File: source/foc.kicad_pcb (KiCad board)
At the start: 2 copper layers, 62.2 x 90.8 mm, 252 parts, among them J1 Conn_01x03, J2 Conn_01x06, J3 Conn_01x08, J4 NRF wireless, J5 Conn_01x04_Male, J6 TYPE-C-31-M-12, P1 SWD, Q1 MMBT5401, Q10 MMBT5401, Q11 CSD19536KCS, Q12 CSD19536KCS, Q2 MMBT5401, Q3 CSD19536KCS, Q4 CSD19536KCS, Q5 MMBT5401, Q6 MMBT5401, Q7 CSD19536KCS, Q8 CSD19536KCS, Q9 MMBT5401, SW1 SW_DPDT_x2, U1 BMI160, U10 TX4130L/PW2902, U11 MS8311, U12 MS8311, U13 MS8311, U14 TJA1050T/CM,118, U15 STM32F405RGT6, U2 AMS1117-3.3, U3 MC74VHC1G66, U4 EG3112, U5 MC74VHC1G66, U6 XL1509-5.0E1, U7 EG3112, U8 MC74VHC1G66, U9 EG3112, Y1 8MHz Crystal Resonator, X5032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

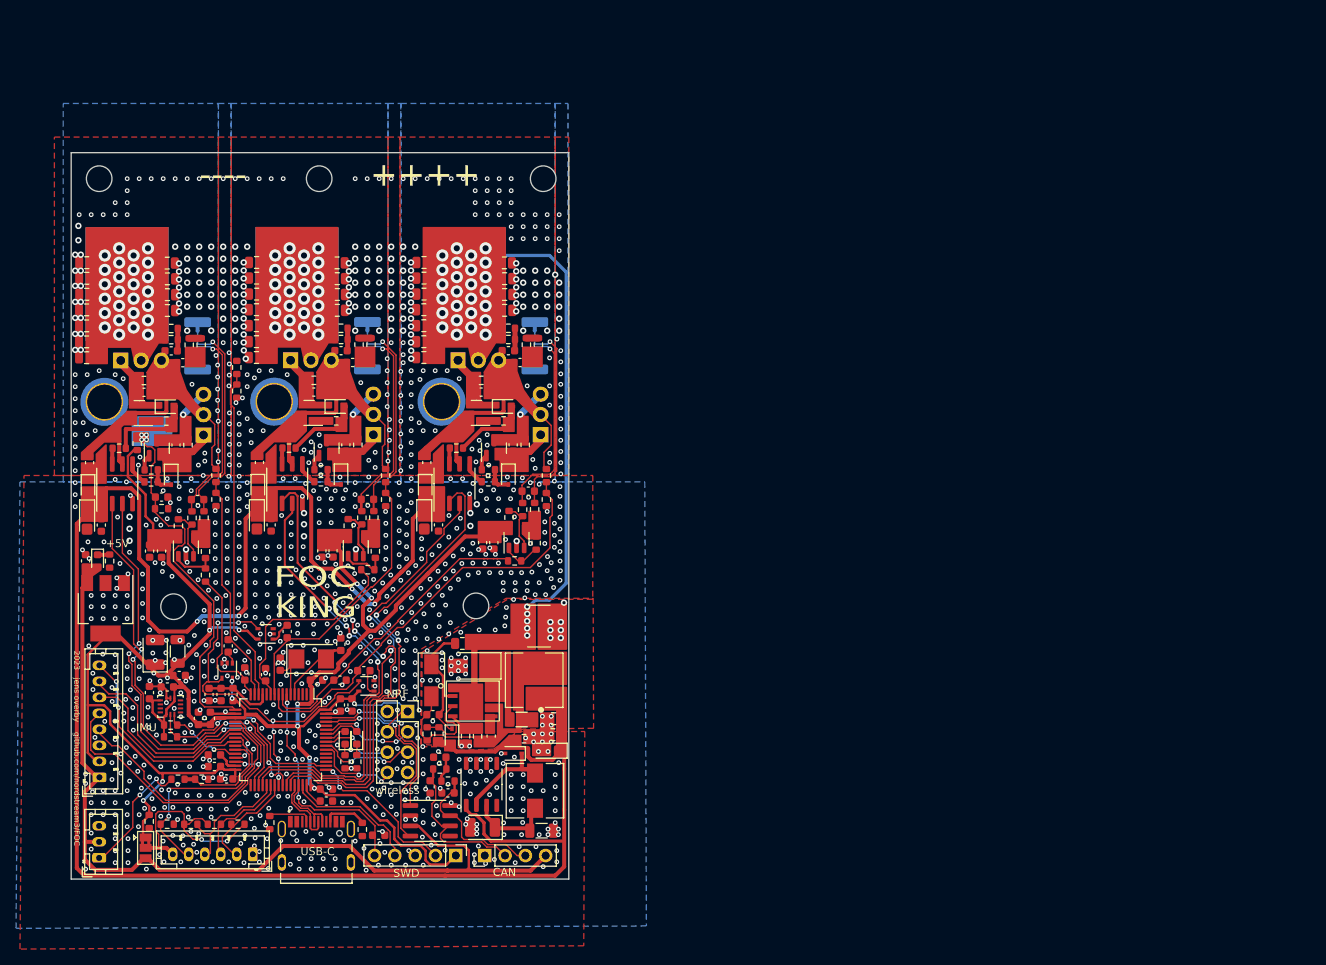
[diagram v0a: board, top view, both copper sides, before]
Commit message: 4 layer design
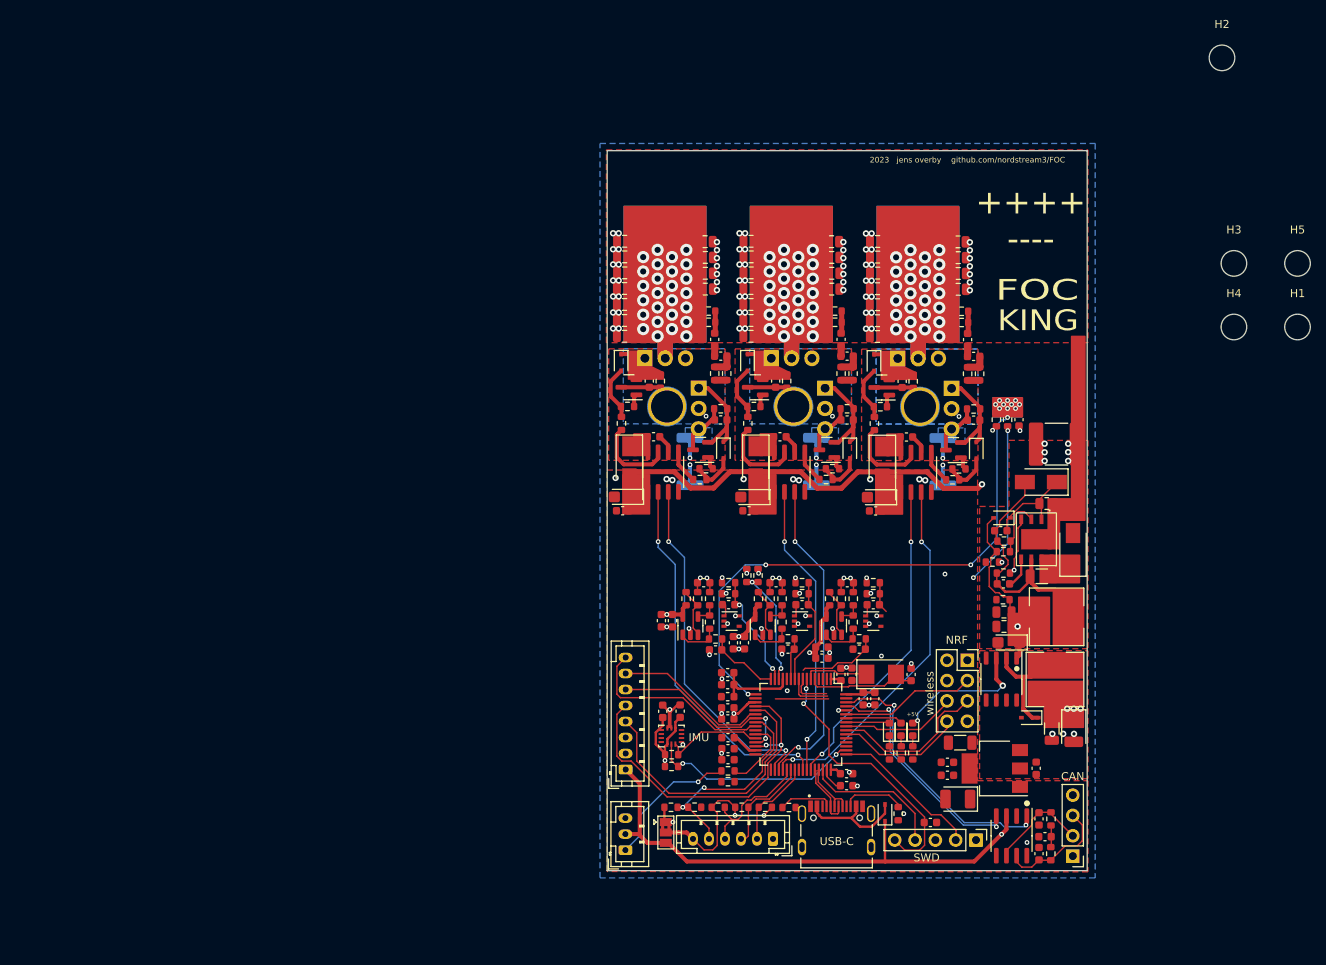
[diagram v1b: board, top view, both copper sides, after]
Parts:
- removed the C13 at (85.2, 105.9)
- removed the C20 at (106.1, 105.9)
- removed the C24 at (106.5, 99.0)
- removed the C33 at (75.1, 96.8)
- removed the C48 at (93.3, 110.0)
- removed the C52 at (92.3, 90.2)
- added C12: 2.2u, Capacitor_SMD:C_0603_1608Metric, F.Cu at (171.5, 136.4)
- added C18: 100n, Capacitor_SMD:C_0603_1608Metric, F.Cu at (162.3, 116.8)
- added C22: 2.2u, Capacitor_SMD:C_0603_1608Metric, F.Cu at (162.6, 105.0)
- added C25: 10u, Capacitor_SMD:C_0603_1608Metric, F.Cu at (166.4, 95.8)
- added C34: 2.2nF, Capacitor_SMD:C_0603_1608Metric, F.Cu at (143.2, 93.7)
- added C51: 1n, Capacitor_SMD:C_0603_1608Metric, F.Cu at (151.6, 122.3)
- added C87: 4.7n, Capacitor_SMD:C_0603_1608Metric, F.Cu at (174.8, 85.7)
- added D15: 1N5819WS, Diode_SMD:D_SOD-323, F.Cu at (163.7, 142.8)
- C11: value 1u -> 10u
- C14: value 100n -> 10u; footprint Capacitor_SMD:C_0603_1608Metric -> Capacitor_Tantalum_SMD:CP_EIA-3216-10_Kemet-I
- C15: value 2.2u -> 100n
- C16: value 1u -> 2.2u
- C17: value 100n -> 10u
- C21: value 2.2u -> 10u; footprint Capacitor_SMD:C_0603_1608Metric -> Capacitor_Tantalum_SMD:CP_EIA-3216-10_Kemet-I
- C49, C69: value 100n -> 2.2u
- C50, C70: value 1n -> 100n
- C54, C73: value 100p -> 2.2nF
- C55, C74: value 100n 100V -> 100p; footprint Capacitor_SMD:C_0805_2012Metric -> Capacitor_SMD:C_0603_1608Metric
- C66, C85: value 4.7n -> 100n 100V; footprint Capacitor_SMD:C_0603_1608Metric -> Capacitor_SMD:C_0805_2012Metric
- C68: value 2.2u -> 4.7n
- C71: value 2.2nF -> 1n
- D1, D3, D6: value 1N4148WS -> US1M; footprint Diode_SMD:D_SOD-323 -> Diode_SMD:D_SMA
- H6: value MountingHole -> Phase_A_Pad; footprint MountingHole:MountingHole_4.3mm_M4_Pad_TopOnly -> Custom:MountingHole_3.5mm_Pad_TopOnly_custom
- H7: value MountingHole -> Phase_B_Pad; footprint MountingHole:MountingHole_4.3mm_M4_Pad_TopOnly -> Custom:MountingHole_3.5mm_Pad_TopOnly_custom
- H8: value MountingHole -> Phase_C_Pad; footprint MountingHole:MountingHole_4.3mm_M4_Pad_TopOnly -> Custom:MountingHole_3.5mm_Pad_TopOnly_custom
- Q11, Q12, Q3, Q4, Q7, Q8: footprint Package_TO_SOT_THT:TO-220-3_Vertical -> Custom:TO-220-3_Vertical_bend
- moved H1 144.8 mm to (215.3, 82.0)
- moved H4 143.0 mm to (207.3, 82.0)
- moved C6 121.6 mm to (182.6, 137.2), turned to 90 degrees
- moved H2 115.7 mm to (205.8, 48.4)
- moved H3 114.8 mm to (207.3, 74.1)
- moved U2 112.9 mm to (177.4, 137.2), turned to 180 degrees
- moved R40 108.8 mm to (179.1, 93.6)
- moved C52 107.6 mm to (180.5, 93.6), turned to 90 degrees
- moved R46 104.9 mm to (177.7, 93.6), turned to 90 degrees
- moved D17 104.0 mm to (167.2, 132.3), turned to 90 degrees
- moved R79 103.2 mm to (167.2, 135.3)
- moved C8 102.0 mm to (172.8, 141.1), turned to 180 degrees
- moved C10 98.5 mm to (173.1, 134.0), turned to 180 degrees
- moved C13 96.8 mm to (171.5, 138.1), turned to 180 degrees
- moved H5 94.9 mm to (215.3, 74.1)
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- renumbered C99 to C100, C100 to C101, C101 to C102, C102 to C103, C103 to C104, C104 to C105, C12 to C13, C18 to C19, C19 to C20, C22 to C23, C23 to C24, C25 to C26, C26 to C27, C27 to C28, C28 to C29, C29 to C30, C30 to C31, C31 to C32, C32 to C33, C34 to C35, C35 to C36, C36 to C37, C37 to C38, C38 to C39, C39 to C40, C40 to C41, C41 to C42, C42 to C43, C43 to C44, C44 to C45, C45 to C46, C46 to C47, C47 to C48, C51 to C52, C87 to C88, C88 to C89, C89 to C90, C90 to C91, C91 to C92, C92 to C93, C93 to C94, C94 to C95, C95 to C96, C96 to C97, C97 to C98, C98 to C99, D15 to D16, D16 to D17
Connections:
- C14 pad 1: /driver/SENS_2 -> +12V
- C15 pad 1: +12V -> /driver/SENS_2
- C15 pad 2: Net-(C13-Pad2) -> Net-(C15-Pad2)
- C16 pad 1: Net-(C16-Pad1) -> +12V
- C16 pad 2: /driver/HS2 -> Net-(C14-Pad2)
- C17 pad 1: /driver/SENS_3 -> Net-(C17-Pad1)
- C17 pad 2: Net-(C17-Pad2) -> /driver/HS2
- C50 pad 2: /mcu/CURRENT_2 -> VCC
- C53 pad 2: Net-(C53-Pad2) -> /driver/HS2
- C55 pad 1: V_IN -> Net-(C55-Pad1)
- C55 pad 2: GND -> Net-(C55-Pad2)
- C66 pad 1: /driver/HS2 -> V_IN
- C66 pad 2: Net-(C66-Pad2) -> GND
- C68 pad 1: VCC -> /driver/HS2
- C68 pad 2: GND -> Net-(C68-Pad2)
- C70 pad 1: GND -> VCC
- C70 pad 2: /mcu/CURRENT_3 -> GND
- C71 pad 1: Net-(C71-Pad1) -> GND
- C71 pad 2: /driver/HS3 -> /mcu/CURRENT_3
- C72 pad 2: Net-(C72-Pad2) -> /driver/HS3
- C74 pad 1: V_IN -> Net-(C74-Pad1)
- C74 pad 2: GND -> Net-(C74-Pad2)
- C85 pad 1: /driver/HS3 -> V_IN
- C85 pad 2: Net-(C85-Pad2) -> GND
- D10 pad 1: Net-(C52-Pad1) -> Net-(C53-Pad1)
- D11 pad 1: Net-(C53-Pad1) -> Net-(C54-Pad1)
- D12 pad 1: Net-(C71-Pad1) -> Net-(C72-Pad1)
- D13 pad 1: Net-(C72-Pad1) -> Net-(C73-Pad1)
- D3 pad 1: Net-(C16-Pad1) -> Net-(C17-Pad1)
- H6 pad 1: (no net) -> /driver/HS1
- H7 pad 1: (no net) -> /driver/HS2
- H8 pad 1: (no net) -> /driver/HS3
- J6 pad A4B9: unconnected-(J6-PadA4B9) -> Net-(D15-Pad2)
- J6 pad B4A9: unconnected-(J6-PadB4A9) -> Net-(D15-Pad2)
- NT3 pad 1: Net-(C54-Pad2) -> Net-(C55-Pad2)
- NT3 pad 2: Net-(C53-Pad2) -> Net-(C54-Pad2)
- NT4 pad 1: Net-(C54-Pad1) -> Net-(C55-Pad1)
- NT5 pad 1: Net-(C73-Pad2) -> Net-(C74-Pad2)
- NT5 pad 2: Net-(C72-Pad2) -> Net-(C73-Pad2)
- NT6 pad 1: Net-(C73-Pad1) -> Net-(C74-Pad1)
- Q10 pad 2: Net-(C72-Pad1) -> Net-(C73-Pad1)
- Q10 pad 3: Net-(C72-Pad2) -> Net-(C73-Pad2)
- Q11 pad 1: Net-(C71-Pad1) -> Net-(C72-Pad1)
- Q12 pad 1: Net-(C72-Pad1) -> Net-(C73-Pad1)
- Q12 pad 3: Net-(C72-Pad2) -> Net-(C73-Pad2)
- Q5 pad 2: Net-(C52-Pad1) -> Net-(C53-Pad1)
- Q6 pad 2: Net-(C53-Pad1) -> Net-(C54-Pad1)
- Q6 pad 3: Net-(C53-Pad2) -> Net-(C54-Pad2)
- Q7 pad 1: Net-(C52-Pad1) -> Net-(C53-Pad1)
- Q8 pad 1: Net-(C53-Pad1) -> Net-(C54-Pad1)
- Q8 pad 3: Net-(C53-Pad2) -> Net-(C54-Pad2)
- Q9 pad 2: Net-(C71-Pad1) -> Net-(C72-Pad1)
- R48 pad 1: Net-(C54-Pad2) -> Net-(C55-Pad2)
- R49 pad 1: Net-(C54-Pad1) -> Net-(C55-Pad1)
- R50 pad 2: Net-(C52-Pad1) -> Net-(C53-Pad1)
- R51 pad 1: Net-(C53-Pad2) -> Net-(C54-Pad2)
- R51 pad 2: Net-(C53-Pad1) -> Net-(C54-Pad1)
- R52 pad 1: Net-(C53-Pad2) -> Net-(C54-Pad2)
- R53 pad 1: Net-(C66-Pad2) -> Net-(C67-Pad2)
- R54 pad 1: Net-(C67-Pad2) -> Net-(C68-Pad2)
- R55 pad 1: Net-(C66-Pad2) -> Net-(C67-Pad2)
- R56 pad 1: Net-(C67-Pad2) -> Net-(C68-Pad2)
- R64 pad 1: Net-(C73-Pad2) -> Net-(C74-Pad2)
- R65 pad 1: Net-(C73-Pad1) -> Net-(C74-Pad1)
- R66 pad 2: Net-(C71-Pad1) -> Net-(C72-Pad1)
- R67 pad 1: Net-(C72-Pad2) -> Net-(C73-Pad2)
- R67 pad 2: Net-(C72-Pad1) -> Net-(C73-Pad1)
- R68 pad 1: Net-(C72-Pad2) -> Net-(C73-Pad2)
- R69 pad 1: Net-(C85-Pad2) -> Net-(C86-Pad2)
- R70 pad 1: Net-(C86-Pad2) -> Net-(C87-Pad2)
- R71 pad 1: Net-(C85-Pad2) -> Net-(C86-Pad2)
- R72 pad 1: Net-(C86-Pad2) -> Net-(C87-Pad2)
- U5 pad 1: Net-(C14-Pad2) -> Net-(C15-Pad2)
- U7 pad 8: Net-(C16-Pad1) -> Net-(C17-Pad1)
- U8 pad 1: Net-(C17-Pad2) -> Net-(C18-Pad2)
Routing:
- net VCC: track 261.4 -> 67.8 mm, vias 13 -> 11
- net +12V: track 265.5 -> 86.3 mm, vias 4 -> 2
- net V_IN: track 75.9 -> 1.63 mm, vias 83 -> 82
- net /driver/SENS_3: track 53.7 -> 9.59 mm
- net /driver/SENS_FILTER: track 47.7 -> 6.65 mm, vias 6 -> 0
- net +5V: track 125.7 -> 86.4 mm, vias 0 -> 6
- net /driver/SENS_SUPPLY: track 41.8 -> 13.7 mm, vias 0 -> 2
- net Net-(C74-Pad2): track 0.00 -> 24.3 mm, vias 0 -> 2
- net /driver/H2: track 60.9 -> 36.8 mm, vias 4 -> 2
- net Net-(C74-Pad1): track 0.00 -> 23.7 mm, vias 0 -> 2
- net /mcu/CURRENT_3: track 38.1 -> 15.0 mm
- net /driver/SENS_2: track 35.6 -> 13.4 mm
- net /mcu/CURRENT_2: track 26.6 -> 5.08 mm
- net Net-(C55-Pad2): track 0.00 -> 21.5 mm, vias 0 -> 2
- net Net-(C54-Pad2): track 28.3 -> 6.79 mm, vias 1 -> 0
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- added copper zone on In2.Cu, net +12V
- added copper zone on In2.Cu, net +5V
- added copper zone on B.Cu, net /driver/HS1
- added copper zone on F.Cu, net /driver/HS1
- added copper zone on B.Cu, net /driver/HS2
- added copper zone on F.Cu, net /driver/HS2
- added copper zone on B.Cu, net /driver/HS3
- added copper zone on F.Cu, net /driver/HS3
- added copper zone on In2.Cu, net GND
- added copper zone on B.Cu, net Net-(C34-Pad2)
- added copper zone on In2.Cu, net VCC
- added copper zone on F.Cu, net V_IN
- added copper zone on In2.Cu, net V_IN
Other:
- board size 62.2 x 90.8 mm -> 60 x 90 mm
- copper layers 2 -> 4

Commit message: Add files via upload
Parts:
- moved H1 84.0 mm to (132.7, 66.7)
- moved H4 66.8 mm to (146.2, 108.9)
- moved H5 55.9 mm to (171.6, 108.9)
- moved H3 47.6 mm to (160.3, 66.7)
- moved H2 27.4 mm to (185.5, 66.7)
- moved C81 13.5 mm to (172.0, 73.4), turned to 0 degrees
- moved C62 13.5 mm to (156.2, 73.4), turned to 0 degrees
- moved C43 9.44 mm to (140.4, 73.4), turned to 0 degrees
- moved C45 4.02 mm to (140.4, 75.3)
- moved C63 4.02 mm to (156.2, 75.3)
- moved C82 3.99 mm to (172.0, 75.3)
- moved C41 3.95 mm to (140.4, 77.2)
- moved C64 3.95 mm to (156.2, 77.2)
- moved C83 3.93 mm to (172.0, 77.2)
- moved R35 3.92 mm to (143.8, 83.3), turned to 90 degrees
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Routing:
- net GND: track 30.7 -> 73.8 mm, vias 112 -> 95
- net Net-(J1-Pad1): track 0.00 -> 17.0 mm, vias 0 -> 1
- net VCC: track 67.8 -> 60.0 mm, vias 11 -> 10
- net V_IN: track 1.63 -> 0.18 mm, vias 82 -> 54
- net /driver/L3: track 45.6 -> 44.7 mm
- added copper zone on B.Cu, net V_IN
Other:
- board size 60 x 90 mm -> 60 x 86.7 mm
- board text added: "+++"
- board text added: "---"
- board text added: "HALL"
- board text added: "SERVO"
- board text removed: "++++"
- board text removed: "----"

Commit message: First 4 layer order at JLCPCB
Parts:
- removed the J4 at (174.0, 123.7)
- moved C69 6.60 mm to (154.9, 116.9)
- moved C49 4.80 mm to (146.0, 116.9), turned to 0 degrees
- moved U5 4.21 mm to (153.7, 123.0)
- moved C15 4.21 mm to (153.7, 121.0)
- moved C70 3.90 mm to (154.9, 118.3)
- moved C9 3.69 mm to (144.7, 120.4)
- moved U3 3.66 mm to (144.8, 122.5)
- moved C50 3.26 mm to (146.0, 118.2), turned to 0 degrees
- moved C18 3.13 mm to (162.4, 119.9)
- moved U8 3.13 mm to (162.4, 121.9)
- moved C32 2.94 mm to (139.6, 122.1)
- moved C51 2.93 mm to (148.7, 122.1)
- moved C71 2.88 mm to (157.6, 122.1)
- moved R9 2.33 mm to (144.7, 113.1), turned to 90 degrees
- moved C30 2.19 mm to (136.9, 116.9), turned to 0 degrees
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- renumbered J5 to J4, J6 to J5
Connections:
- C14 pad 2: Net-(C14-Pad2) -> GND
- C16 pad 2: Net-(C14-Pad2) -> GND
- U15 pad 29: /mcu/TX_SCL_MOSI -> unconnected-(U15-Pad29)
- U15 pad 30: /mcu/RX_SDA_NSS -> unconnected-(U15-Pad30)
- U15 pad 54: /mcu/NRF_MISO -> unconnected-(U15-Pad54)
- U15 pad 55: /mcu/NRF_MOSI -> unconnected-(U15-Pad55)
- U15 pad 56: /mcu/NRF_SCK -> unconnected-(U15-Pad56)
- U15 pad 59: /mcu/NRF_CSN -> unconnected-(U15-Pad59)
- U15 pad 8: /mcu/CURRENT_3 -> /driver/SENS_3
- U15 pad 9: /driver/SENS_3 -> /mcu/CURRENT_3
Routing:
- net V_IN: track 0.18 -> 41.5 mm, vias 54 -> 60
- net /driver/SENS_FILTER: track 6.65 -> 37.2 mm, vias 0 -> 6
- net /mcu/NRF_MOSI: track 19.9 -> 0.00 mm
- net +5V: track 86.4 -> 103.9 mm, vias 6 -> 8
- net /mcu/NRF_CSN: track 16.9 -> 0.00 mm
- net /mcu/NRF_MISO: track 15.9 -> 0.00 mm
- net /mcu/NRF_SCK: track 14.4 -> 0.00 mm
- net /driver/SENS_3: track 9.59 -> 21.7 mm
- net +12V: track 86.3 -> 95.9 mm
- net GND: track 73.8 -> 65.7 mm, vias 95 -> 215
- net VCC: track 60.0 -> 55.2 mm, vias 10 -> 17
- net /mcu/CURRENT_3: track 15.0 -> 10.6 mm
- net Net-(CYA0650-68UH1-Pad1): track 13.5 -> 17.0 mm
- net Net-(C74-Pad2): track 24.3 -> 27.5 mm
- net Net-(C74-Pad1): track 23.7 -> 26.8 mm
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- added copper zone on In1.Cu, net GND
- added copper zone on F.Cu, net VCC
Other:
- board text removed: "NRF"
- board text removed: "wireless"

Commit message: Add files via upload
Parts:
- removed the C33 at (134.3, 88.8)
- removed the C47 at (141.1, 84.9)
- removed the C48 at (143.2, 85.7)
- removed the C65 at (156.2, 79.1)
- removed the C66 at (156.2, 81.0)
- removed the C67 at (156.9, 84.9)
- removed the C68 at (159.0, 85.7)
- removed the C72 at (165.9, 88.8)
- removed the C73 at (174.8, 93.7)
- removed the C86 at (172.7, 84.9)
- removed the C87 at (174.8, 85.7)
- removed the H3 at (160.3, 66.7)
- removed the H7 at (152.3, 92.0)
- removed the R37 at (142.4, 83.3)
- removed the R38 at (142.4, 87.9)
- removed the R43 at (146.6, 94.1)
- removed the R44 at (156.4, 101.1)
- removed the R53 at (159.6, 83.3)
- removed the R54 at (159.7, 87.9)
- removed the R55 at (158.2, 83.3)
- removed the R56 at (158.2, 87.9)
- removed the R67 at (174.8, 92.3)
- removed the R69 at (175.4, 83.3)
- removed the R70 at (175.6, 87.9)
- removed the R71 at (174.0, 83.3)
- removed the R72 at (174.1, 87.9)
- added C35: 100n 100V, Capacitor_SMD:C_0805_2012Metric, F.Cu at (132.1, 75.5)
- added C52: 100n 100V, Capacitor_SMD:C_0805_2012Metric, F.Cu at (148.3, 73.5)
- added C55: 100n 100V, Capacitor_SMD:C_0805_2012Metric, F.Cu at (148.3, 79.2)
- added C80: 4.7n, Capacitor_SMD:C_0603_1608Metric, F.Cu at (170.1, 83.2)
- added C81: 4.7n, Capacitor_SMD:C_0603_1608Metric, F.Cu at (171.0, 85.2)
- added H5: Phase_A_Pad, Custom:MountingHole_3.5mm_Pad_TopOnly_custom, B.Cu at (136.8, 92.3)
- added R39: 0R, Resistor_SMD:R_0603_1608Metric, F.Cu at (147.9, 92.5)
- added R40: 2.2R, Resistor_SMD:R_0603_1608Metric, F.Cu at (156.8, 99.9)
- added R48: ASR-M-3-0.25F 0.25mR, Resistor_SMD:R_2512_6332Metric, B.Cu at (158.7, 84.8)
- added R49: 10R, Resistor_SMD:R_0603_1608Metric, F.Cu at (152.2, 81.1)
- added R63: 10R, Resistor_SMD:R_0603_1608Metric, F.Cu at (168.4, 81.0)
- added R64: 10R, Resistor_SMD:R_0603_1608Metric, F.Cu at (172.2, 82.5)
- added R65: 10R, Resistor_SMD:R_0603_1608Metric, F.Cu at (168.4, 82.4)
- C34, C53, C54: value 2.2nF -> 100n 100V; footprint Capacitor_SMD:C_0603_1608Metric -> Capacitor_SMD:C_0805_2012Metric
- C45, C46, C63, C64: value 100n 100V -> 4.7n; footprint Capacitor_SMD:C_0805_2012Metric -> Capacitor_SMD:C_0603_1608Metric
- H6: value Phase_A_Pad -> Phase_B_Pad
- R24: value 2k2 -> 0R
- R25, R42: value 2k2 -> 2.2R
- R27: value 4.7R -> 2.2R
- R32: value 4.7k @ 75v -> ASR-M-3-0.25F 0.25mR; footprint Resistor_SMD:R_0603_1608Metric -> Resistor_SMD:R_2512_6332Metric; moved to B.Cu
- R33, R50, R51, R66: value 4.7k @ 75v -> 10R
- R34, R52: value ASR-M-3-0.25F 0.25mR -> 10R; footprint Resistor_SMD:R_2512_6332Metric -> Resistor_SMD:R_0603_1608Metric; moved to F.Cu
- R41: value 2k2 -> 4.7R
- R54: renamed from R58; value 2k2 -> 0R
- R55: renamed from R59; value 2k2 -> 2.2R
- R57: renamed from R61; value 4.7R -> 2.2R
- moved C50 50.5 mm to (141.2, 125.4)
- moved R44 49.3 mm to (139.9, 125.4)
- moved R38 35.5 mm to (143.9, 98.8)
- moved C34 22.9 mm to (132.1, 73.6)
- moved C54 19.5 mm to (148.3, 77.3)
- moved NT6 19.4 mm to (174.9, 82.3), turned to 90 degrees
- moved NT4 19.2 mm to (158.7, 82.4), turned to 90 degrees
- moved NT2 19.0 mm to (142.5, 82.5), turned to 90 degrees
- moved H3 18.8 mm to (136.5, 125.3)
- moved H6 16.5 mm to (153.0, 92.2)
- moved H4 16.2 mm to (173.0, 125.4)
- moved R34 16.1 mm to (139.6, 82.7), turned to 0 degrees
- moved R52 14.9 mm to (156.0, 84.0), turned to 0 degrees
- moved R62 14.7 mm to (174.9, 84.8), turned to 90 degrees
- moved C53 13.5 mm to (148.3, 75.4), turned to 180 degrees
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- renumbered C35 to C33, C49 to C47, C50 to C48, C51 to C49, C52 to C50, C55 to C51, C69 to C65, C70 to C66, C71 to C67, C74 to C68, C75 to C69, C76 to C70, C77 to C71, C78 to C72, C79 to C73, C80 to C74, C81 to C75, C82 to C76, C83 to C77, C84 to C78, C85 to C79, C88 to C82, C89 to C83, C90 to C84, C91 to C85, C92 to C86, C93 to C87, C94 to C88, C95 to C89, C96 to C90, C97 to C91, C98 to C92, C99 to C93, C100 to C94, C101 to C95, C102 to C96, C103 to C97, C104 to C98, C105 to C99, H4 to H3, H5 to H4, H8 to H7, R39 to R37, R40 to R38, R45 to R43, R46 to R44, R47 to R45, R48 to R46, R49 to R47, R57 to R53, R60 to R56, R62 to R58, R63 to R59, R64 to R60, R65 to R61, R68 to R62, R73 to R67, R74 to R68, R75 to R69, R76 to R70, R77 to R71, R78 to R72, R79 to R73
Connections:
- C34 pad 1: Net-(C34-Pad1) -> V_IN
- C34 pad 2: Net-(C34-Pad2) -> GND
- C45 pad 1: V_IN -> /driver/HS1
- C45 pad 2: GND -> Net-(C45-Pad2)
- C46 pad 1: V_IN -> /driver/HS1
- C46 pad 2: GND -> Net-(C46-Pad2)
- C53 pad 1: Net-(C53-Pad1) -> V_IN
- C53 pad 2: /driver/HS2 -> GND
- C54 pad 1: Net-(C54-Pad1) -> V_IN
- C54 pad 2: Net-(C54-Pad2) -> GND
- C63 pad 1: V_IN -> /driver/HS2
- C63 pad 2: GND -> Net-(C63-Pad2)
- C64 pad 1: V_IN -> /driver/HS2
- C64 pad 2: GND -> Net-(C64-Pad2)
- D10 pad 1: Net-(C53-Pad1) -> Net-(D10-Pad1)
- D11 pad 1: Net-(C54-Pad1) -> Net-(D11-Pad1)
- D12 pad 1: Net-(C72-Pad1) -> Net-(D12-Pad1)
- D8 pad 1: Net-(C33-Pad1) (its old number) -> Net-(D8-Pad1)
- D9 pad 1: Net-(C34-Pad1) -> Net-(D9-Pad1)
- H6 pad 1: /driver/HS1 -> /driver/HS2
- NT1 pad 2: Net-(C34-Pad2) -> Net-(NT1-Pad2)
- NT3 pad 2: Net-(C54-Pad2) -> Net-(NT3-Pad2)
- Q1 pad 2: Net-(C33-Pad1) (its old number) -> Net-(D8-Pad1)
- Q11 pad 1: Net-(C72-Pad1) -> Net-(D12-Pad1)
- Q2 pad 2: Net-(C34-Pad1) -> Net-(D9-Pad1)
- Q2 pad 3: Net-(C34-Pad2) -> Net-(NT1-Pad2)
- Q3 pad 1: Net-(C33-Pad1) (its old number) -> Net-(D8-Pad1)
- Q4 pad 1: Net-(C34-Pad1) -> Net-(D9-Pad1)
- Q4 pad 3: Net-(C34-Pad2) -> Net-(NT1-Pad2)
- Q5 pad 2: Net-(C53-Pad1) -> Net-(D10-Pad1)
- Q6 pad 2: Net-(C54-Pad1) -> Net-(D11-Pad1)
- Q6 pad 3: Net-(C54-Pad2) -> Net-(NT3-Pad2)
- Q7 pad 1: Net-(C53-Pad1) -> Net-(D10-Pad1)
- Q8 pad 1: Net-(C54-Pad1) -> Net-(D11-Pad1)
- Q8 pad 3: Net-(C54-Pad2) -> Net-(NT3-Pad2)
- Q9 pad 2: Net-(C72-Pad1) -> Net-(D12-Pad1)
- R32 pad 1: /driver/HS1 -> Net-(NT1-Pad2)
- R32 pad 2: Net-(C33-Pad1) (its old number) -> GND
- R33 pad 1: Net-(C34-Pad2) -> Net-(C45-Pad2)
- R33 pad 2: Net-(C34-Pad1) -> V_IN
- R34 pad 1: Net-(C34-Pad2) -> Net-(C46-Pad2)
- R35 pad 1: Net-(C47-Pad2) -> Net-(C45-Pad2)
- R36 pad 1: Net-(C48-Pad2) -> Net-(C46-Pad2)
- R41 pad 1: Net-(Q5-Pad1) -> /driver/HO2
- R42 pad 1: Net-(Q6-Pad1) -> /driver/LO2
- R50 pad 1: /driver/HS2 -> Net-(C64-Pad2)
- R50 pad 2: Net-(C53-Pad1) -> GND
- R51 pad 1: Net-(C54-Pad2) -> Net-(C63-Pad2)
- R51 pad 2: Net-(C54-Pad1) -> V_IN
- R52 pad 1: Net-(C54-Pad2) -> Net-(C64-Pad2)
- R66 pad 1: /driver/HS3 -> Net-(C81-Pad2)
- R66 pad 2: Net-(C72-Pad1) -> GND
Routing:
- net /mcu/ADC_TEMP: track 67.7 -> 37.4 mm, vias 14 -> 11
- net Net-(C33-Pad1): track 17.7 -> 33.5 mm
- net Net-(C51-Pad1): track 21.6 -> 36.6 mm
- net Net-(C51-Pad2): track 21.9 -> 36.1 mm
- net Net-(C33-Pad2): track 19.0 -> 33.0 mm
- net V_IN: track 41.5 -> 28.0 mm, vias 60 -> 53
- net Net-(C34-Pad1): track 13.1 -> 0.00 mm
- net Net-(C54-Pad1): track 13.1 -> 0.00 mm
- net Net-(C68-Pad1): track 26.8 -> 39.6 mm
- net Net-(NT1-Pad2): track 0.00 -> 12.0 mm, vias 0 -> 1
- net Net-(NT3-Pad2): track 0.00 -> 12.0 mm, vias 0 -> 1
- net Net-(C68-Pad2): track 27.5 -> 39.1 mm
- net /driver/HS3: track 34.1 -> 45.5 mm, vias 2 -> 1
- net Net-(C53-Pad1): track 8.96 -> 0.00 mm
- net Net-(C72-Pad1): track 8.96 -> 0.00 mm
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- added copper zone on B.Cu, net Net-(NT1-Pad2)
- added copper zone on B.Cu, net Net-(NT3-Pad2)
- added copper zone on B.Cu, net Net-(NT5-Pad2)
- removed copper zone on B.Cu, net /driver/HS1
- removed copper zone on B.Cu, net /driver/HS2
- removed copper zone on B.Cu, net /driver/HS3
- removed copper zone on B.Cu, net Net-(C34-Pad2)
